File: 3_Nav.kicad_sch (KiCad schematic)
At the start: 49 parts, among them J401 Screw_Terminal_01x04, Q401 Si2302_NMOS, SW401 SW_Push, SW402 SW_Push, U401 LPS22HH, U402 MS5607, U403 STM32F412RGTx, U404 ICM-42688-P, U405 LSM6DSO32TR, Y401 YXC YSX321SL, Y402 ABRACON ABS05

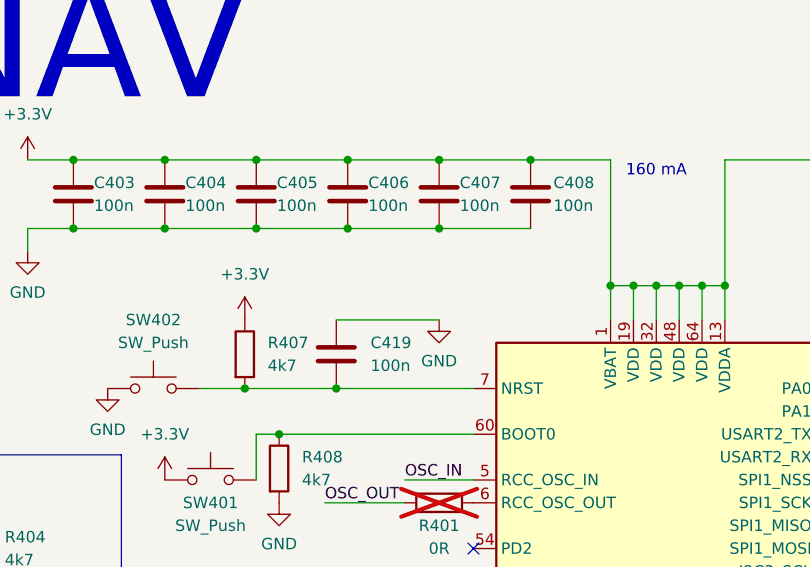
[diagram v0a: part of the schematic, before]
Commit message: Corrected power section for the billionth time Added programming notes
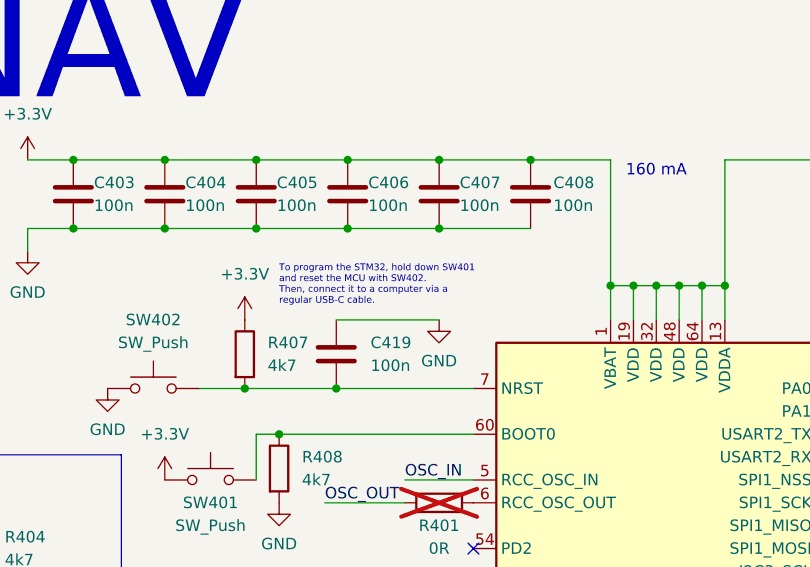
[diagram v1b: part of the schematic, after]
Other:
- note added: "To program the STM32, hold down SW401 and reset the MCU with SW402. Then, connect it to a computer via a regular USB-C cable."
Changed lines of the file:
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@@
+		)
+	)
+	(text "To program the STM32, hold down SW401 \nand reset the MCU with SW402.\nThen, connect it to a computer via a \nregular USB-C cable."
+		(exclude_from_sim no)
+		(at 95.25 60.96 0)
+		(effects
+			(font
+				(face "Arial")
+				(size 0.75 0.75)
+			)
+			(justify left)
 		)
 	)

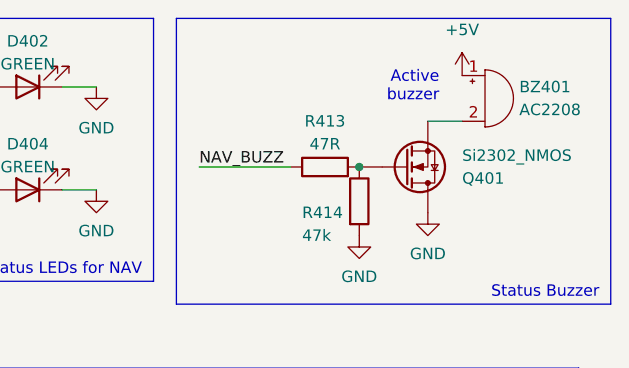
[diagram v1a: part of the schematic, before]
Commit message: Added Title Block
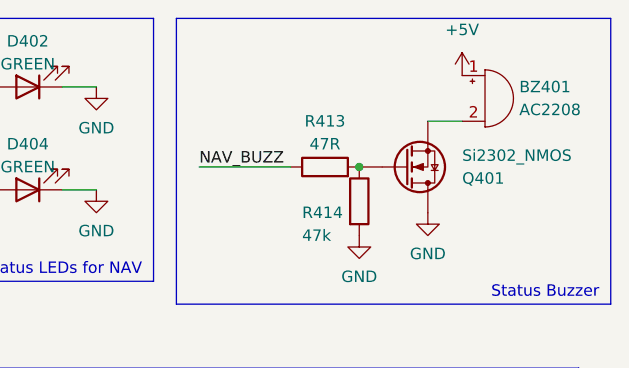
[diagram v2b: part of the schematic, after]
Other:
- note removed: "Active buzzer"
- title: (none) -> Polaris/NAV
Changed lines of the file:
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@@
 	(generator_version "10.0")
 	(paper "A4")
+	(title_block
+		(title "Polaris/NAV")
+	)
 	(rectangle
 		(start 189.992 51.562)
@@
 		)
 	)
-	(text "Active\nbuzzer"
-		(exclude_from_sim no)
-		(at 265.43 20.32 0)
-		(effects
-			(font
-				(size 1.27 1.27)
-			)
-			(justify right)
-		)
-	)

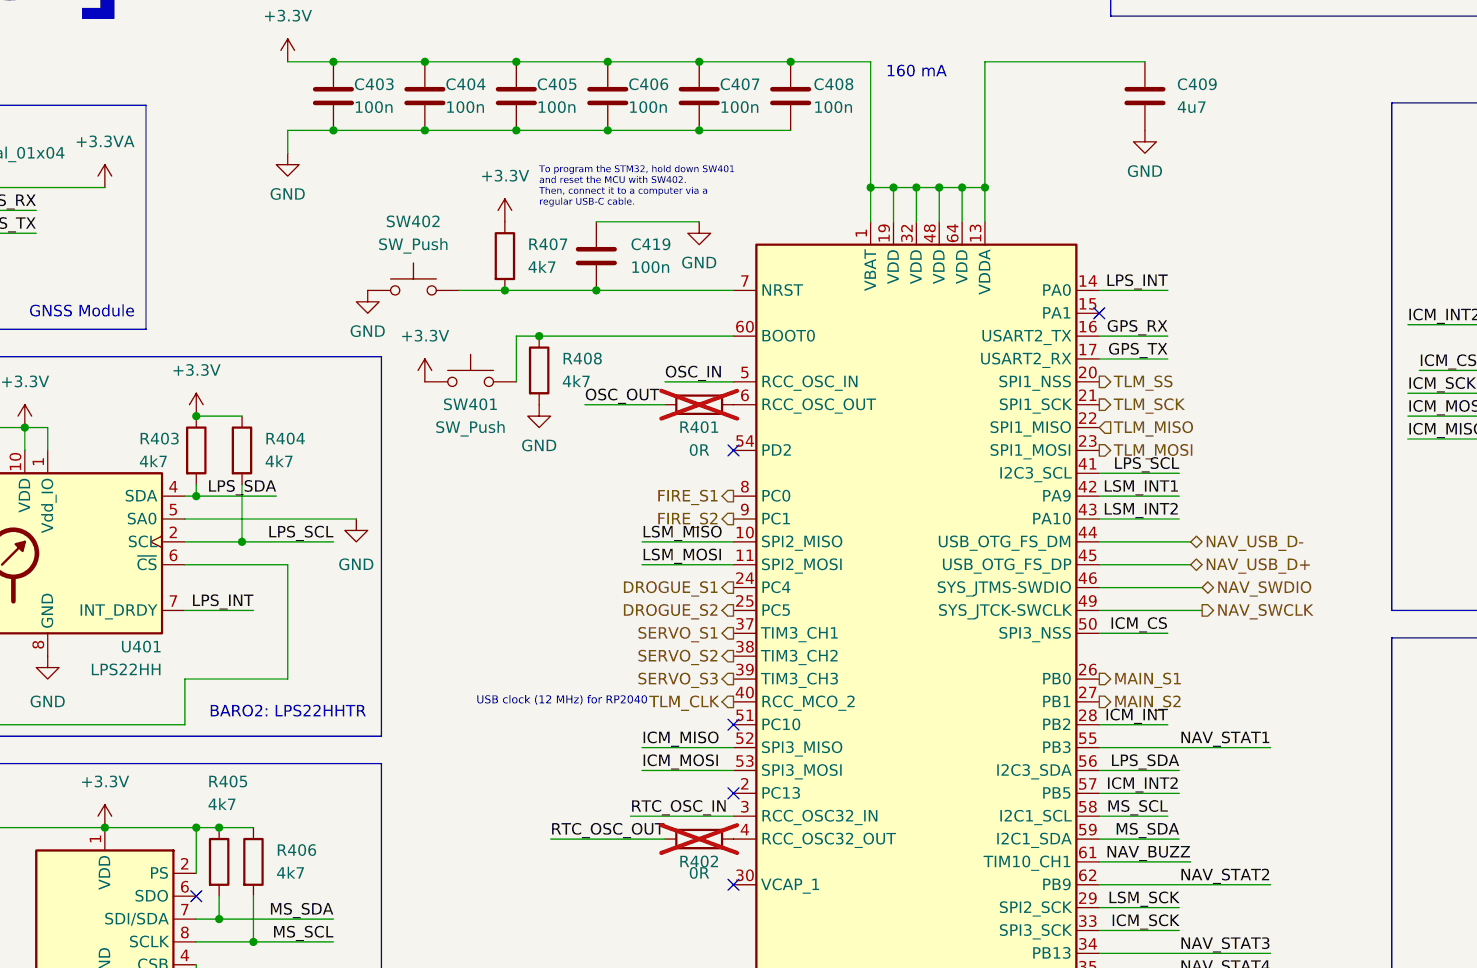
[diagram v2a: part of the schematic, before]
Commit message: Broke out remaining GPIO pins of NAV
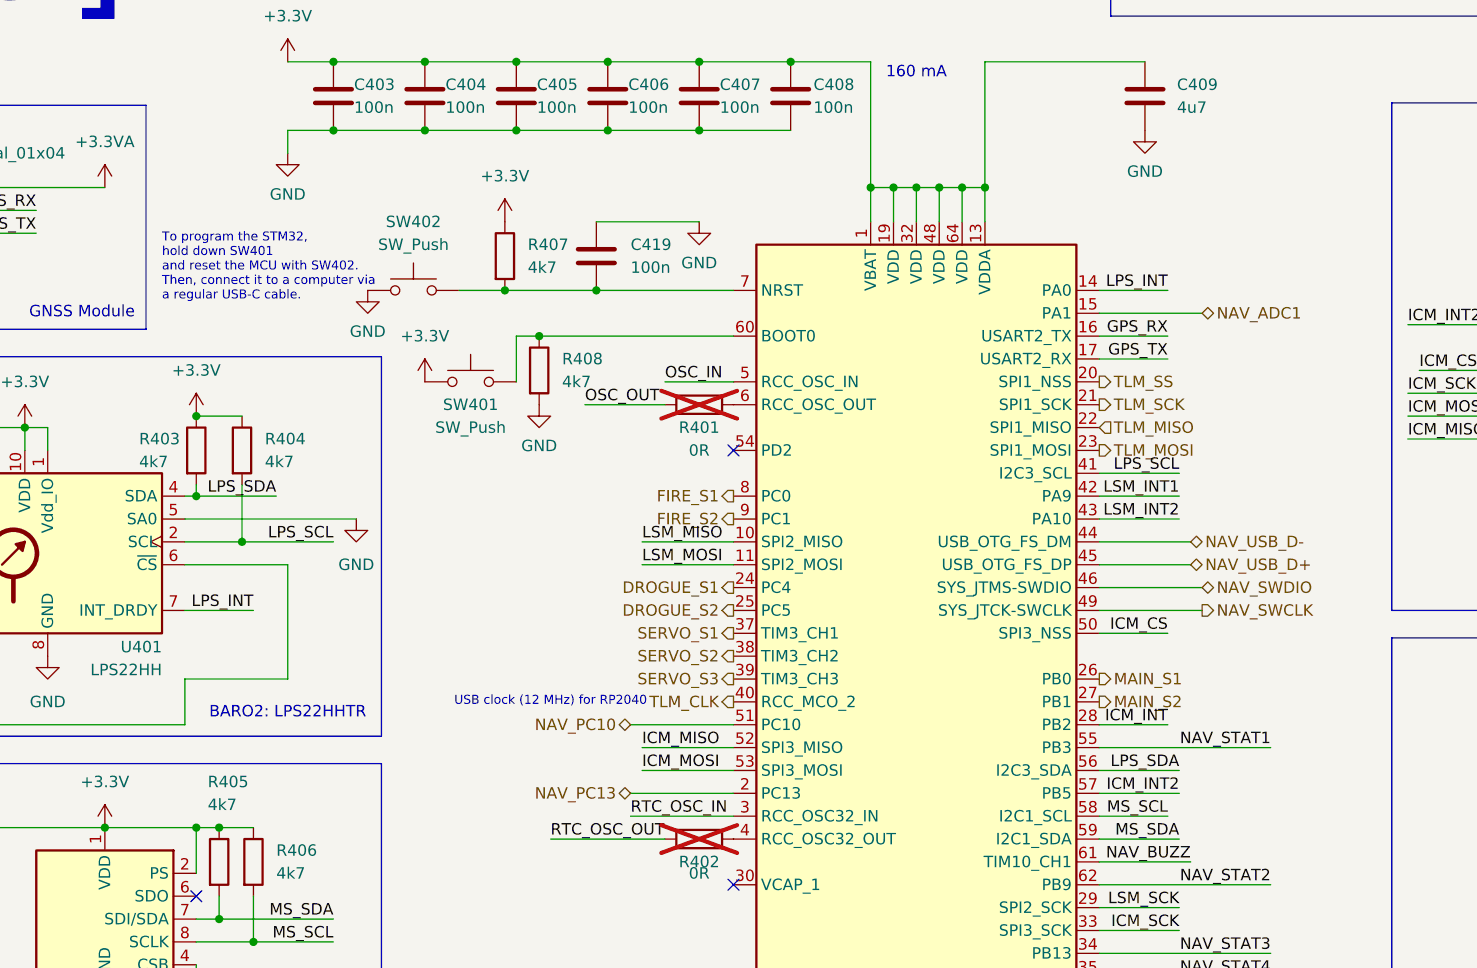
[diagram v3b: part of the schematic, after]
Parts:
- BZ401: footprint (none) -> Polaris:AC1255
- C419: footprint (none) -> Capacitor_SMD:C_0603_1608Metric
- Q401: footprint (none) -> Package_TO_SOT_SMD:SOT-23
- R413, R414: footprint (none) -> Resistor_SMD:R_0603_1608Metric
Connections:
- net NAV_ADC1: now reaches U403.15 (PA1)
- net NAV_PC13: now reaches U403.2 (PC13)
- net NAV_PC10: now reaches U403.51 (PC10)
- no-connect marks 6 -> 3

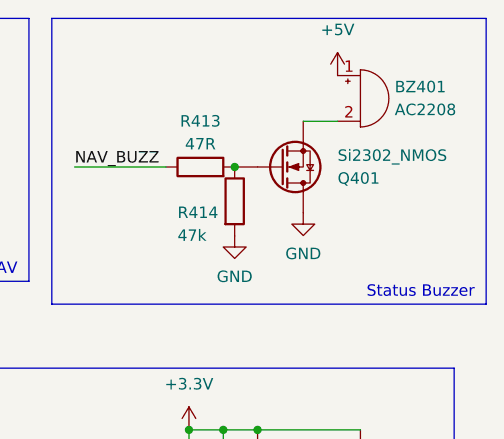
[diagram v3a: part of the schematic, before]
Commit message: Finally started the PCB layout and routing Only took me a few decades Also labeled some unlabeled nets in the schematic Changed the USB mux to be two 1x3 pin headers instead of one 2x3 Edited symbols and footprints to match pin numbers
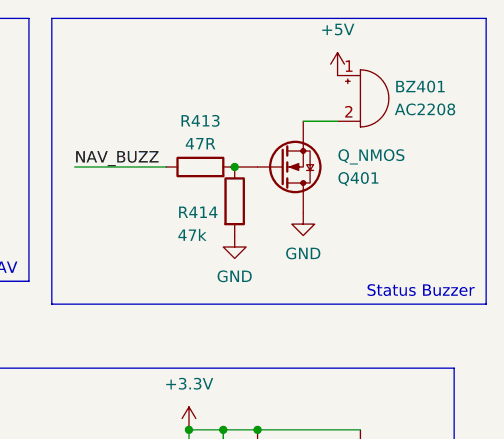
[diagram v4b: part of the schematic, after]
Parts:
- Q401: value Si2302_NMOS -> Q_NMOS
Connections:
- net GND: now also Q401.3 (D); no longer Q401.D
- net at R413.2, R414.1: now also Q401.1 (G); no longer Q401.G
- net at BZ401.2 (-): now also Q401.2 (S); no longer Q401.S
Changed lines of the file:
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@@
 			)
 		)
-		(property "Value" "Si2302_NMOS"
+		(property "Value" "Q_NMOS"
 			(at 267.97 27.9401 0)
 			(show_name no)
@@
 		)
 		(property "Footprint" "Package_TO_SOT_SMD:SOT-23"
-			(at 266.7 31.75 0)
+			(at 267.97 13.97 0)
 			(hide yes)
 			(show_name no)
@@
 		)
 		(property "Description" "N-MOSFET transistor"
-			(at 261.62 29.21 0)
+			(at 261.62 43.18 0)
 			(hide yes)
 			(show_name no)
@@
 			)
 		)
-		(pin "D"
+		(pin "3"
 		)
-		(pin "S"
+		(pin "2"
 		)
-		(pin "G"
+		(pin "1"
 		)
 		(instances

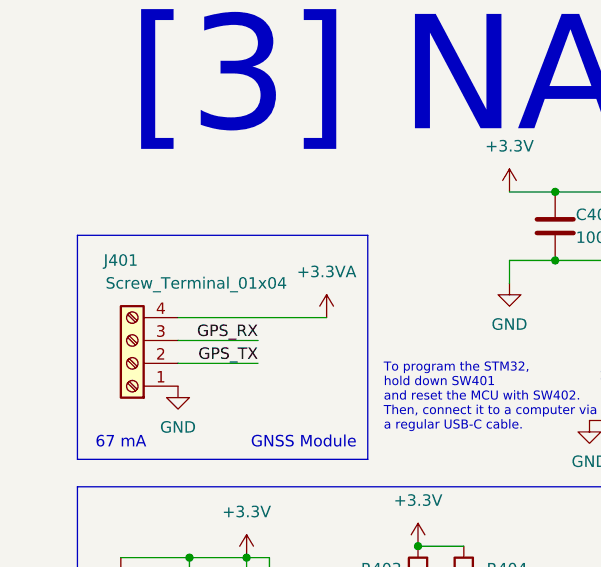
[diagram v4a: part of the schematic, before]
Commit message: Renamed a few nets
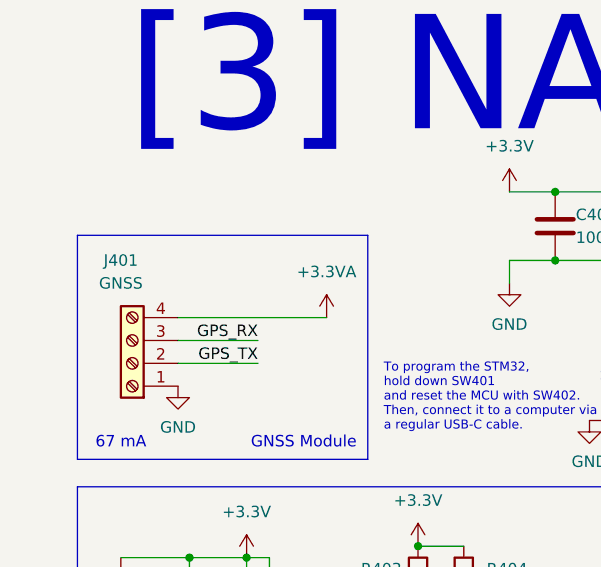
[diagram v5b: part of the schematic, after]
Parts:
- J401: value Screw_Terminal_01x04 -> GNSS
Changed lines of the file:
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@@
 			)
 		)
-		(property "Value" "Screw_Terminal_01x04"
-			(at 32.512 57.15 0)
+		(property "Value" "GNSS"
+			(at 24.13 57.15 0)
 			(show_name no)
 			(do_not_autoplace no)

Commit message: Redesigned the whole thing for the hundredth time
Changed from dual MCU to single MCU
Changed main MCU to STM32F446VE
Added CubeMX project (ioc) file for easy access to pinouts
Note: The PCB file still contains the previous connections and footprints
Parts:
- removed R402: 0R, Resistor_SMD:R_0603_1608Metric, symbol Device:R
- removed U403: STM32F412RGTx, Package_QFP:LQFP-64_10x10mm_P0.5mm, symbol MCU_ST_STM32F4:STM32F412RGTx
- removed Y402: ABRACON ABS05, Crystal:Crystal_SMD_3215-2Pin_3.2x1.5mm, symbol Device:Crystal
- added C420, C422, C423: 100n, Capacitor_SMD:C_0603_1608Metric, symbol Device:C
- added C421: 10u, Capacitor_SMD:C_0805_2012Metric, symbol Device:C
- added C424: 47u, Capacitor_SMD:C_0805_2012Metric, symbol Device:C
- added D405: D_TVS, LED_SMD:LED_0603_1608Metric, symbol Device:D_TVS
- added J402: Conn_Coaxial, Connector_Coaxial:SMA_Molex_73251-2200_Horizontal, symbol Connector:Conn_Coaxial
- added R415: 10k, Resistor_SMD:R_0603_1608Metric, symbol Device:R
- added R416: 810k, Resistor_SMD:R_0603_1608Metric, symbol Device:R
- added U403: STM32F446VETx, Package_QFP:LQFP-100_14x14mm_P0.5mm, symbol MCU_ST_STM32F4:STM32F446VETx
- added U406: W25Q128JVE, Package_SON:WSON-8-1EP_8x6mm_P1.27mm_EP3.4x4.3mm, symbol Memory_Flash:W25Q128JVE
- added U407: THD-2528-11SD-GF, Polaris:TF-SMD_THD2528-11SD-GF, symbol Polaris_symbols:MicroSD_THD2528-11SD-GF
- added U408: Ra-08H, Polaris:RA-08H, symbol Polaris_symbols:Ai-Thinker_Ra-08H
- C417, C418: value 12p -> 100n
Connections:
- net RTC_OSC_IN is gone; now on net +3.3V: C418.1
- net RTC_OSC_OUT is gone; now on net +3.3V: C417.1
- net +3.3V: now also C420.1, C421.1, C422.1, U403.100 (VDD), U403.11 (VDD), U403.19 (VDD), U403.22 (VDDA), U403.28 (VDD), U403.50 (VDD), U403.6 (VBAT), U403.75 (VDD), U406.8 (VCC), U407.4 (VDD)
- net +3.3VA: now also C423.1, C424.1, D405.2 (A2), R415.1, R416.1, U408.9 (VCC)
- net GND: now also C420.2, C421.2, C422.2, C423.2, C424.2, D405.1 (A1), J402.2 (Ext), U403.10 (VSS), U403.20 (VSSA), U403.27 (VSS), U403.49 (VSS), U403.74 (VSS), U403.99 (VSS), U406.4 (GND), U406.9 (EP), U407.10 (SHELL), U407.11 (SHELL), U407.12 (SHELL), U407.13 (SHELL), U407.6 (VSS), U408.1 (GND), U408.17 (GND)
- net GPS_RX: now also U403.23 (PA0)
- net GPS_TX: now also U403.24 (PA1)
- net ICM_CS: now also U403.51 (PB12)
- net ICM_MISO: now also U403.17 (PC2)
- net ICM_MOSI: now also U403.16 (PC1)
- net ICM_SCK: now also U403.52 (PB13)
- net LPS_SCL: now also U403.67 (PA8)
- net LPS_SDA: now also U403.66 (PC9)
- net LSM_MISO: now also U403.31 (PA6)
- net LSM_MOSI: now also U403.32 (PA7)
- net LSM_SCK: now also U403.30 (PA5)
- net MS_SCL: now also U403.95 (PB8)
- net MS_SDA: now also U403.93 (PB7)
- net OSC_IN: now also U403.12 (PH0)
- net SERVO_S1: now also U403.54 (PB15)
- net SERVO_S2: now also U403.40 (PE9)
- net SERVO_S3: now also U403.42 (PE11)
- net SERVO_S4: now also U403.44 (PE13)
- net at R408.1, SW401.2: now also U403.94 (BOOT0)
- net at C419.2, R407.2, SW402.2: now also U403.14 (NRST)
- net at R401.2: now also U403.13 (PH1)
- net ICM_INT2: no longer names the net of U404.9 (INT2/FSYNC/CLKIN)
- net LSM_INT2: no longer names the net of U405.9 (INT2)
- new net: J402.1 (In), U408.18 (ANT)
- new net FLASH_CLK: U403.84 (PD3), U406.6 (CLK)
- new net FLASH_CS: U403.92 (PB6), U406.1 (~{CS})
- new net FLASH_IO0: U403.58 (PD11), U406.5 (DI/IO_{0})
- new net FLASH_IO1: U403.59 (PD12), U406.2 (DO/IO_{1})
- new net FLASH_IO2: U403.1 (PE2), U406.3 (~{WP}/IO_{2})
- new net FLASH_IO3: U403.60 (PD13), U406.7 (~{HOLD}/~{RESET}/IO_{3})
- new net RF_BOOT: R415.2, U408.15 (BOOT)
- new net RF_RESET: R416.2, U408.16 (RESET)
- new net RF_RX: U403.39 (PE8), U408.10 (LPRXD)
- new net RF_TX: U403.38 (PE7), U408.11 (UART_TX)
- new net SD_CD: U407.9 (CD)
- new net SD_CLK: U403.37 (PB2), U407.5 (CLK)
- new net SD_CMD: U403.83 (PD2), U407.3 (CMD)
- new net SD_DAT0: U403.65 (PC8), U407.7 (DAT0)
- new net SD_DAT1: U403.35 (PB0), U407.8 (DAT1)
- new net SD_DAT2: U403.36 (PB1), U407.1 (DAT2)
- new net SD_DAT3: U403.79 (PC11), U407.2 (DAT3)
- new net SERVO_S0: U403.53 (PB14)
- new net SERVO_S5: U403.45 (PE14)
- new net USB_D+: U403.71 (PA12)
- new net USB_D-: U403.70 (PA11)
- no-connect marks 3 -> 13
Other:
- note added: "240 mA"
- note added: "500mA"
- note added: "QSPI: Flash SDIO: SD card SPI1: LSM6DSO32 SPI2: ICM-42688-P I2C1: MS5607 I2C3: LPS22HH UART4: GNSS Module UART5: LoRa Radio"
- note removed: "160 mA"
- note removed: "32.768 kHz Crystal (for RTC)"
- note removed: "9 pF Load capacitance"
- note removed: "SPI1: RP2040 SPI2: LSM6DSO32 SPI3: ICM-42688-P I2C1: MS5607 I2C3: LPS22HH USART2: GPS NEO-M8N"
- note removed: "USB clock (12 MHz) for RP2040"
- moved on the sheet: BZ401, C401, C402, C403, C404, C405, C406, C407, C408, C409, C410, C411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

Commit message: Switched main 3.3V LDO to a modern part
New one: TLV75733
Old one: NCP1117
New one has cleaner output, lower dropout voltage and is cheaper.

Also continued completing the connections for NAV
Updated README to include changes to architecture
Also updated pin connections on CubeMX (ioc) file
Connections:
- net LSM_INT1 is gone; now on net LSM_INT: U405.4 (INT1)
- net DROGUE_S0: now also U403.61 (PD14)
- net DROGUE_S1: now also U403.62 (PD15)
- net FIRE_S0: now also U403.63 (PC6)
- net FIRE_S1: now also U403.64 (PC7)
- net ICM_CS: now also U403.29 (PA4); no longer U403.51 (PB12)
- net ICM_INT: now also U403.26 (PA3)
- net ICM_MISO: now also U403.32 (PA7); no longer U403.17 (PC2)
- net ICM_MOSI: now also U403.31 (PA6); no longer U403.16 (PC1)
- net ICM_SCK: now also U403.30 (PA5); no longer U403.52 (PB13)
- net LPS_INT: now also U403.68 (PA9)
- net LSM_INT: now also U403.51 (PB12)
- net LSM_MISO: now also U403.17 (PC2); no longer U403.31 (PA6)
- net LSM_MOSI: now also U403.16 (PC1); no longer U403.32 (PA7)
- net LSM_SCK: now also U403.52 (PB13); no longer U403.30 (PA5)
- net MAIN_S0: now also U403.56 (PD9)
- net MAIN_S1: now also U403.57 (PD10)
- net NAV_BUZZ: now also U403.81 (PD0)
- net NAV_STAT1: now also U403.85 (PD4)
- net NAV_STAT2: now also U403.86 (PD5)
- net NAV_STAT3: now also U403.87 (PD6)
- net NAV_STAT4: now also U403.88 (PD7)
- net SD_CD: now also U403.82 (PD1)
- net SPI4_NSS: now reaches U403.3 (PE4)
- net SPI4_MISO: now reaches U403.4 (PE5)
- net SPI4_SCK: now reaches U403.43 (PE12)
- net I2C2_SCL: now reaches U403.47 (PB10)
- net SPI4_MOSI: now reaches U403.5 (PE6)
- net PC13: now reaches U403.7 (PC13)
- net SYS_SWDIO: now reaches U403.72 (PA13)
- net SYS_SWCLK: now reaches U403.76 (PA14)
- net PC14: now reaches U403.8 (PC14)
- net I2C2_SDA: now reaches U403.80 (PC12)
- net PC15: now reaches U403.9 (PC15)
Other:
- moved on the sheet: C410, C411, C412, C413, C414, U404, U405
